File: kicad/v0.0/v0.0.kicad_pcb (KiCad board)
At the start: 2 copper layers, 62 parts, among them J1 USB_B_Micro, J2 9V_IN, J3 LED, J4 MOTOR, J5 LED, J6 MOTOR, Q1 IRF520, Q2 IRF520, SW1 SW_Push, SW2 SW_Push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

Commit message: forgot to save | ready to design PCB
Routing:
- net /3V3: track 34.5 -> 0.00 mm
- net (no net): track 0.00 -> 0.55 mm

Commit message: ab to start pcb design
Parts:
- moved TP5 43.3 mm to (115.0, 88.0)
- moved TP10 42.8 mm to (115.0, 93.0)
- moved TP6 37.5 mm to (119.5, 93.2)
- moved TP9 37.1 mm to (119.5, 97.9)
- moved TP3 37.1 mm to (115.0, 97.8)
- moved TP4 36.9 mm to (119.7, 88.2)
- moved J3 36.2 mm to (204.0, 96.7)
- moved TP7 35.4 mm to (127.9, 88.2)
- moved TP12 33.3 mm to (123.7, 88.0)
- moved U3 32.7 mm to (235.7, 82.5)
- moved TP1 30.6 mm to (123.7, 93.0)
- moved TP2 30.1 mm to (123.7, 98.0)
- moved TP11 28.8 mm to (128.0, 93.1)
- moved TP8 27.5 mm to (128.0, 98.0)
- moved C4 25.1 mm to (275.0, 87.5)
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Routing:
- net +9V: track 56.2 -> 5.74 mm
- net Net-(D5-Pad1): track 35.1 -> 5.32 mm
- net +5V: track 12.9 -> 3.95 mm

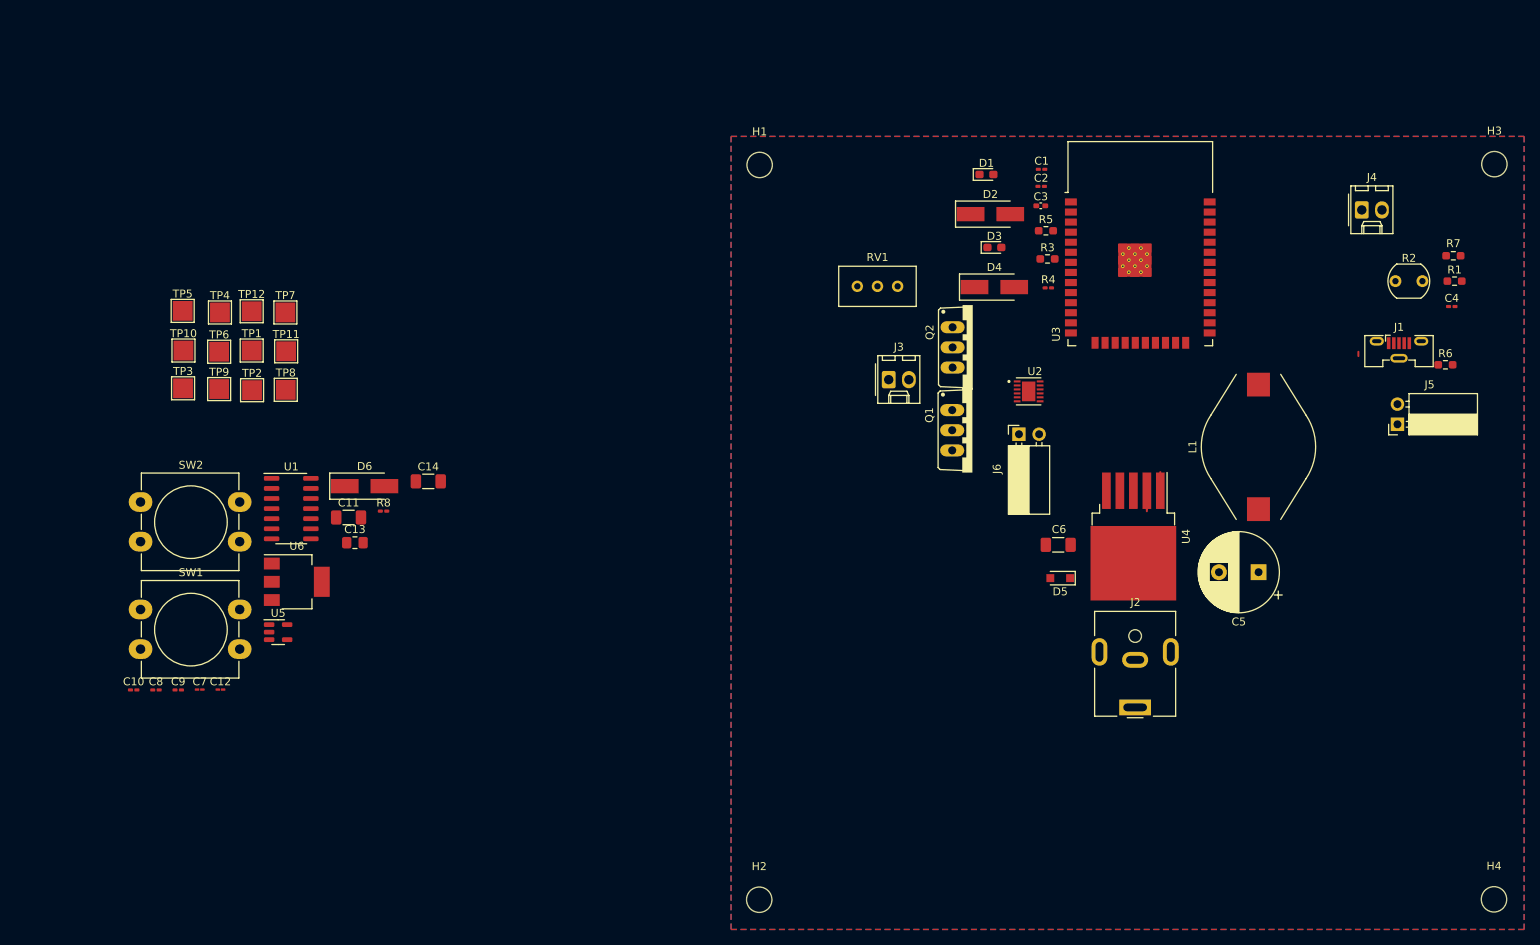
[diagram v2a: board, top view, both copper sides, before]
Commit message: pcb is laid out, time to route
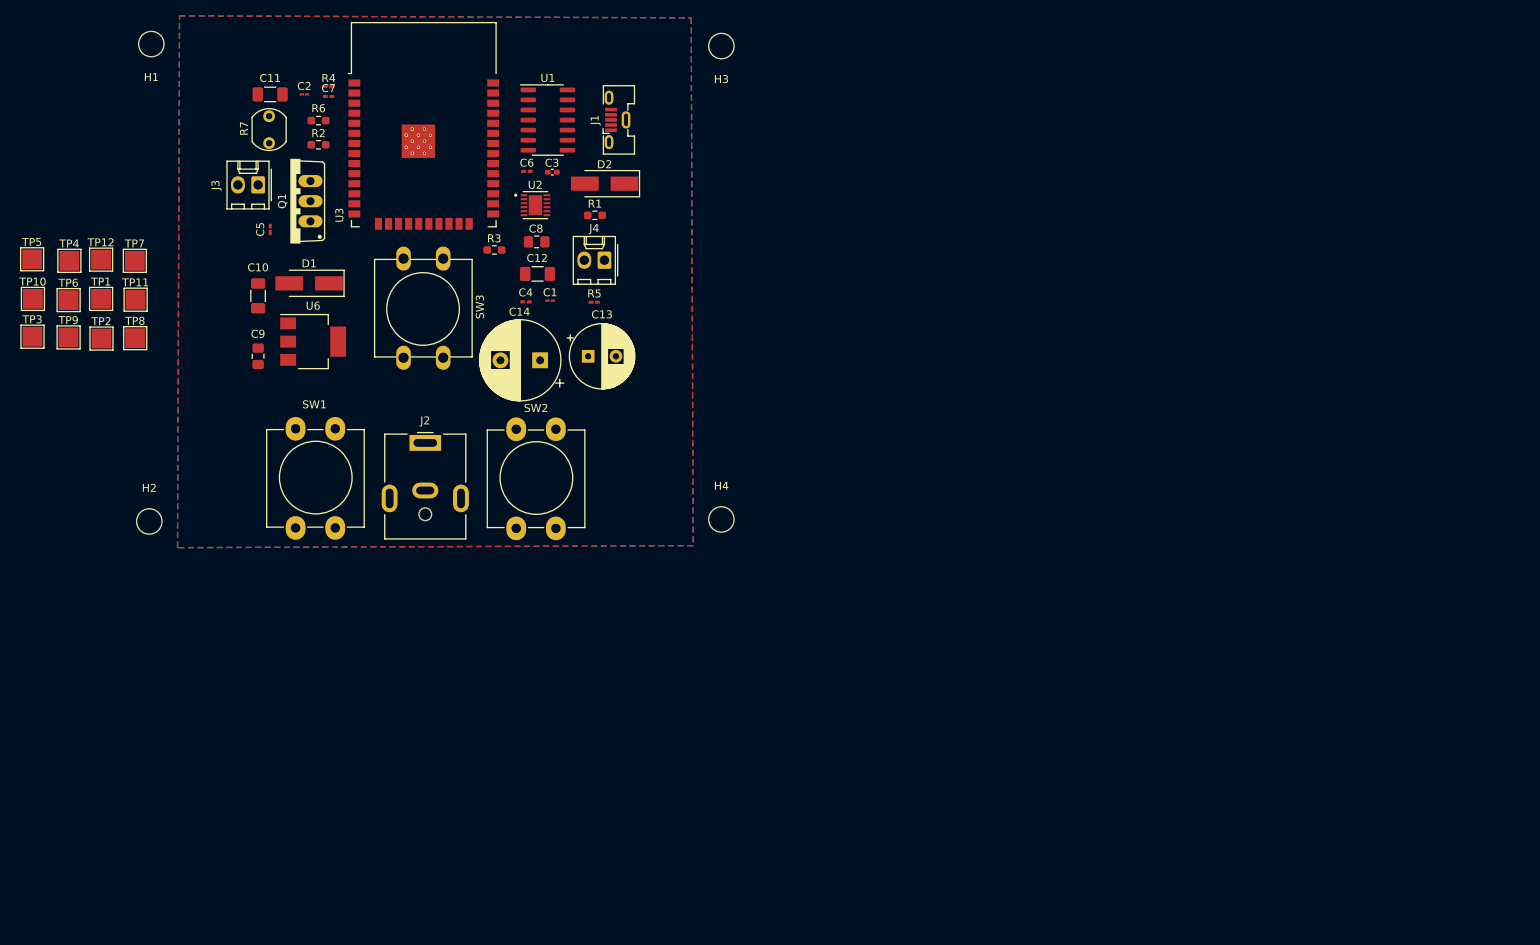
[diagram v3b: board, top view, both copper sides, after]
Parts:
- removed D3: LED, LED_SMD:LED_0603_1608Metric_Pad1.05x0.95mm_HandSolder
- removed D4, D6: D, Diode_SMD:D_SMA_Handsoldering
- removed D5: D_Schottky, Diode_SMD:D_SOD-323_HandSoldering
- removed J5: LED, Connector_PinSocket_2.54mm:PinSocket_1x02_P2.54mm_Horizontal
- removed J6: MOTOR, Connector_PinSocket_2.54mm:PinSocket_1x02_P2.54mm_Horizontal
- removed L1: 68u, Inductor_SMD:L_Bourns_SDR1806
- removed Q2: IRF520, IRF520:TO220BV
- removed R8: 10k, Resistor_SMD:R_0201_0603Metric_Pad0.64x0.40mm_HandSolder
- removed RV1: 100k, Potentiometer_THT:Potentiometer_Bourns_3296W_Vertical
- removed U4: LM2596S-5, Package_TO_SOT_SMD:TO-263-5_TabPin3
- removed U5: AP2112K-3.3, Package_TO_SOT_SMD:SOT-23-5
- added SW3: OPEN/CLOSE, Button_Switch_THT:SW_PUSH-12mm, F.Cu at (147.8, 81.4)
- C1, C2: value 1u -> .1u; footprint Capacitor_SMD:C_0201_0603Metric_Pad0.64x0.40mm_HandSolder -> Capacitor_SMD:C_01005_0402Metric_Pad0.57x0.30mm_HandSolder
- C10: value 1u -> 22u; footprint Capacitor_SMD:C_0201_0603Metric_Pad0.64x0.40mm_HandSolder -> Capacitor_SMD:C_1206_3216Metric_Pad1.33x1.80mm_HandSolder
- C12: value .1u -> 22u; footprint Capacitor_SMD:C_01005_0402Metric_Pad0.57x0.30mm_HandSolder -> Capacitor_SMD:C_1206_3216Metric_Pad1.33x1.80mm_HandSolder
- C13: value 10u -> 220u; footprint Capacitor_SMD:C_0805_2012Metric_Pad1.18x1.45mm_HandSolder -> Capacitor_THT:CP_Radial_D8.0mm_P3.50mm
- C14: value 22u -> 470u; footprint Capacitor_SMD:C_1206_3216Metric_Pad1.33x1.80mm_HandSolder -> Capacitor_THT:CP_Radial_D10.0mm_P5.00mm
- C5: value 470u -> 1u; footprint Capacitor_THT:CP_Radial_D10.0mm_P5.00mm -> Capacitor_SMD:C_0201_0603Metric_Pad0.64x0.40mm_HandSolder
- C6: value 220u -> 1u; footprint Capacitor_SMD:C_1206_3216Metric_Pad1.33x1.80mm_HandSolder -> Capacitor_SMD:C_0201_0603Metric_Pad0.64x0.40mm_HandSolder
- C7: value .1u -> 1u; footprint Capacitor_SMD:C_01005_0402Metric_Pad0.57x0.30mm_HandSolder -> Capacitor_SMD:C_0201_0603Metric_Pad0.64x0.40mm_HandSolder
- C8, C9: value 1u -> 10u; footprint Capacitor_SMD:C_0201_0603Metric_Pad0.64x0.40mm_HandSolder -> Capacitor_SMD:C_0805_2012Metric_Pad1.18x1.45mm_HandSolder
- D1: value LED -> D; footprint LED_SMD:LED_0603_1608Metric_Pad1.05x0.95mm_HandSolder -> Diode_SMD:D_SMA_Handsoldering
- R1: value 20k -> 1k
- R2: value R_Photo -> 1k; footprint OptoDevice:R_LDR_5.1x4.3mm_P3.4mm_Vertical -> Resistor_SMD:R_0603_1608Metric_Pad0.98x0.95mm_HandSolder
- R5: value 1k -> 10k; footprint Resistor_SMD:R_0603_1608Metric_Pad0.98x0.95mm_HandSolder -> Resistor_SMD:R_0201_0603Metric_Pad0.64x0.40mm_HandSolder
- R6: value 1k -> 20k
- R7: value 1k -> R_Photo; footprint Resistor_SMD:R_0603_1608Metric_Pad0.98x0.95mm_HandSolder -> OptoDevice:R_LDR_5.1x4.3mm_P3.4mm_Vertical
- SW1: value SW_Push -> RST
- SW2: value SW_Push -> FLASH
- moved R7 150.4 mm to (125.8, 63.5), turned to -90 degrees
- moved R6 145.4 mm to (132.1, 64.0)
- moved R2 136.9 mm to (132.1, 67.1)
- moved C5 131.9 mm to (126.0, 77.7), turned to -90 degrees
- moved C4 116.7 mm to (158.2, 86.9), turned to 180 degrees
- moved R1 108.7 mm to (166.9, 76.0)
- moved H4 108.6 mm to (182.9, 114.3)
- moved J1 102.7 mm to (169.8, 63.9), turned to 90 degrees
- moved H3 98.6 mm to (182.9, 54.6), turned to 180 degrees
- moved J4 95.7 mm to (168.1, 81.6), turned to 180 degrees
- moved J2 95.5 mm to (145.5, 104.6), turned to 0 degrees
- moved R4 94.2 mm to (133.3, 59.7)
- moved C2 93.6 mm to (130.3, 60.7), turned to 180 degrees
- moved U3 91.6 mm to (145.3, 67.5)
- moved Q1 90.7 mm to (128.5, 74.2), turned to 90 degrees
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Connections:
- net /flash renamed Net-(SW2-Pad1)
- C1 pad 1: Net-(C1-Pad1) -> +9V
- C10 pad 1: Net-(C10-Pad1) -> Net-(D1-Pad2)
- C12 pad 1: +3V3 -> +9V
- C14 pad 1: Net-(C14-Pad1) -> +9V
- C2 pad 1: +9V -> +3V3
- C5 pad 1: GND -> +9V
- C5 pad 2: +9V -> GND
- C6 pad 1: +5V -> Net-(C6-Pad1)
- C8 pad 1: Net-(C7-Pad1) -> +9V
- C9 pad 1: +5V -> +9V
- D1 pad 1: GND -> +3V3
- J1 pad 1: Net-(C1-Pad1) -> Net-(C6-Pad1)
- R1 pad 1: Net-(R1-Pad1) -> /SNS
- R2 pad 1: +3V3 -> Net-(R6-Pad1)
- R2 pad 2: Net-(R1-Pad1) -> /V_PHOTO
- R3 pad 1: /SNS -> GND
- R3 pad 2: GND -> Net-(SW3-Pad1)
- R4 pad 1: Net-(R4-Pad1) -> +3V3
- R4 pad 2: GND -> Net-(C7-Pad1)
- R5 pad 2: Net-(D1-Pad2) -> GND
- R6 pad 2: Net-(D3-Pad2) -> GND
- R7 pad 1: Net-(R1-Pad1) -> +3V3
- R7 pad 2: /V_PHOTO -> Net-(R6-Pad1)
- U1 pad 1: Net-(C1-Pad1) -> Net-(C6-Pad1)
- U1 pad 2: Net-(R6-Pad1) -> unconnected-(U1-Pad2)
- U1 pad 3: Net-(R5-Pad1) -> unconnected-(U1-Pad3)
- U2 pad 8: Net-(R4-Pad1) -> Net-(R5-Pad1)
- U3 pad 27: /open/close button (input) -> Net-(SW3-Pad1)
- U3 pad 28: /led (output) -> /LED
- U3 pad 30: /FWD -> /REV
- U3 pad 31: /REV -> /FWD
- U6 pad 2: Net-(C14-Pad1) -> Net-(D1-Pad2)
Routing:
- net +9V: track 5.74 -> 0.00 mm
- net Net-(D5-Pad1): track 5.32 -> 0.00 mm
- net +5V: track 3.95 -> 0.00 mm
- net Net-(SW3-Pad1): track 0.00 -> 1.11 mm
- net +3V3: track 0.00 -> 0.89 mm
- net (no net): track 0.55 -> 0.00 mm

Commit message: minor tweaks, im a lil bit of a control freak so i keep messing wit it
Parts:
- moved R2 0.76 mm to (132.1, 67.8)
- moved C7 0.60 mm to (133.3, 61.6)
- moved R6 0.51 mm to (132.1, 64.5)
- moved R4 0.25 mm to (133.3, 59.4)
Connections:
- R3 pad 2: Net-(SW3-Pad1) -> Net-(R3-Pad2)
- SW3 pad 1: Net-(SW3-Pad1) -> GND
- U3 pad 27: Net-(SW3-Pad1) -> Net-(R3-Pad2)
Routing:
- net Net-(SW3-Pad1): track 1.11 -> 0.00 mm
- net GND: track 0.00 -> 1.11 mm
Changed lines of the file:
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@@
   (net 63 "unconnected-(U3-Pad36)")
   (net 64 "unconnected-(U3-Pad37)")
-  (net 65 "Net-(SW3-Pad1)")
-  (net 66 "Net-(SW2-Pad1)")
-  (net 67 "Net-(R6-Pad1)")
-  (net 68 "Net-(R5-Pad1)")
-  (net 69 "unconnected-(U1-Pad2)")
-  (net 70 "unconnected-(U1-Pad3)")
+  (net 65 "Net-(SW2-Pad1)")
+  (net 66 "Net-(R6-Pad1)")
+  (net 67 "Net-(R5-Pad1)")
+  (net 68 "unconnected-(U1-Pad2)")
+  (net 69 "unconnected-(U1-Pad3)")
+  (net 70 "Net-(R3-Pad2)")
   (footprint "Capacitor_SMD:C_0201_0603Metric_Pad0.64x0.40mm_HandSolder" (layer "F.Cu")
     (at 125.984 77.724 -90)
@@
     (fp_line (start 12.25 -3.5) (end 12.25 8.5) (layer "F.Fab") (width 0.1))
     (pad "1" thru_hole oval (at 12.5 0 270) (size 3.048 1.85) (drill 1.3) (layers *.Cu *.Mask)
-      (net 65 "Net-(SW3-Pad1)") (pinfunction "1") (pintype "passive"))
+      (net 2 "GND") (pinfunction "1") (pintype "passive"))
     (pad "1" thru_hole oval (at 0 0 270) (size 3.048 1.85) (drill 1.3) (layers *.Cu *.Mask)
-      (net 65 "Net-(SW3-Pad1)") (pinfunction "1") (pintype "passive"))
+      (net 2 "GND") (pinfunction "1") (pintype "passive"))
     (pad "2" thru_hole oval (at 0 5 270) (size 3.048 1.85) (drill 1.3) (layers *.Cu *.Mask)
       (net 9 "+3V3") (pinfunction "2") (pintype "passive"))
@@
   )
   (footprint "Resistor_SMD:R_0603_1608Metric_Pad0.98x0.95mm_HandSolder" (layer "F.Cu")
-    (at 132.08 64.008)
+    (at 132.08 64.516)
     (descr "Resistor SMD 0603 (1608 Metric), square (rectangular) end terminal, IPC_7351 nominal with elongated pad for handsoldering. (Body size source: IPC-SM-782 page 72, https://www.pcb-3d.com/wordpress/wp-content/uploads/ipc-sm-782a_amendment_1_and_2.pdf), generated with kicad-footprint-generator")
     (tags "resistor handsolder")
@@
     (fp_line (start -0.8 0.4125) (end -0.8 -0.4125) (layer "F.Fab") (width 0.1))
     (pad "1" smd roundrect (at -0.9125 0) (size 0.975 0.95) (layers "F.Cu" "F.Paste" "F.Mask") (roundrect_rratio 0.25)
-      (net 67 "Net-(R6-Pad1)") (pintype "passive"))
+      (net 66 "Net-(R6-Pad1)") (pintype "passive"))
     (pad "2" smd roundrect (at 0.9125 0) (size 0.975 0.95) (layers "F.Cu" "F.Paste" "F.Mask") (roundrect_rratio 0.25)
       (net 2 "GND") (pintype "passive"))
@@
       (net 59 "Net-(C6-Pad1)") (pinfunction "VDD") (pintype "power_in"))
     (pad "2" smd roundrect (at -2.475 -2.54) (size 1.95 0.6) (layers "F.Cu" "F.Paste" "F.Mask") (roundrect_rratio 0.25)
-      (net 69 "unconnected-(U1-Pad2)") (pinfunction "GP0") (pintype "bidirectional"))
+      (net 68 "unconnected-(U1-Pad2)") (pinfunction "GP0") (pintype "bidirectional"))
     (pad "3" smd roundrect (at -2.475 -1.27) (size 1.95 0.6) (layers "F.Cu" "F.Paste" "F.Mask") (roundrect_rratio 0.25)
-      (net 70 "unconnected-(U1-Pad3)") (pinfunction "GP1") (pintype "bidirectional"))
+      (net 69 "unconnected-(U1-Pad3)") (pinfunction "GP1") (pintype "bidirectional"))
     (pad "4" smd roundrect (at -2.475 0) (size 1.95 0.6) (layers "F.Cu" "F.Paste" "F.Mask") (roundrect_rratio 0.25)
       (net 31 "unconnected-(U1-Pad4)") (pinfunction "~{RST}") (pintype "input"))
@@
     (fp_line (start 0.25 -3.5) (end 0.25 8.5) (layer "F.Fab") (width 0.1))
     (pad "1" thru_hole oval (at 12.5 0 90) (size 3 2.5) (drill 1.2) (layers *.Cu *.Mask)
-      (net 66 "Net-(SW2-Pad1)") (pinfunction "1") (pintype "passive"))
+      (net 65 "Net-(SW2-Pad1)") (pinfunction "1") (pintype "passive"))
     (pad "1" thru_hole oval (at 0 0 90) (size 3 2.5) (drill 1.2) (layers *.Cu *.Mask)
-      (net 66 "Net-(SW2-Pad1)") (pinfunction "1") (pintype "passive"))
+      (net 65 "Net-(SW2-Pad1)") (pinfunction "1") (pintype "passive"))
     (pad "2" thru_hole oval (at 12.5 5 90) (size 3 2.5) (drill 1.2) (layers *.Cu *.Mask)
       (net 2 "GND") (pinfunction "2") (pintype "passive"))
@@
       (net 2 "GND") (pintype "passive"))
     (pad "2" smd roundrect (at 0.9125 0 180) (size 0.975 0.95) (layers "F.Cu" "F.Paste" "F.Mask") (roundrect_rratio 0.25)
-      (net 65 "Net-(SW3-Pad1)") (pintype "passive"))
+      (net 70 "Net-(R3-Pad2)") (pintype "passive"))
     (model "${KICAD6_3DMODEL_DIR}/Resistor_SMD.3dshapes/R_0603_1608Metric.wrl"
       (offset (xyz 0 0 0))
@@
   )
   (footprint "Capacitor_SMD:C_0201_0603Metric_Pad0.64x0.40mm_HandSolder" (layer "F.Cu")
-    (at 133.35 60.96 180)
+    (at 133.35 61.564 180)
     (descr "Capacitor SMD 0201 (0603 Metric), square (rectangular) end terminal, IPC_7351 nominal with elongated pad for handsoldering. (Body size source: https://www.vishay.com/docs/20052/crcw0201e3.pdf), generated with kicad-footprint-generator")
     (tags "capacitor handsolder")
@@
     (pad "" smd roundrect (at 0.4325 0) (size 0.458 0.36) (layers "F.Paste") (roundrect_rratio 0.25))
     (pad "1" smd roundrect (at -0.4075 0) (size 0.635 0.4) (layers "F.Cu" "F.Mask") (roundrect_rratio 0.25)
-      (net 68 "Net-(R5-Pad1)") (pintype "passive"))
+      (net 67 "Net-(R5-Pad1)") (pintype "passive"))
     (pad "2" smd roundrect (at 0.4075 0) (size 0.635 0.4) (layers "F.Cu" "F.Mask") (roundrect_rratio 0.25)
       (net 2 "GND") (pintype "passive"))
@@
   )
   (footprint "Resistor_SMD:R_0603_1608Metric_Pad0.98x0.95mm_HandSolder" (layer "F.Cu")
-    (at 132.08 67.056)
+    (at 132.08 67.818)
     (descr "Resistor SMD 0603 (1608 Metric), square (rectangular) end terminal, IPC_7351 nominal with elongated pad for handsoldering. (Body size source: IPC-SM-782 page 72, https://www.pcb-3d.com/wordpress/wp-content/uploads/ipc-sm-782a_amendment_1_and_2.pdf), generated with kicad-footprint-generator")
     (tags "resistor handsolder")
@@
     (fp_line (start 0.8 -0.4125) (end 0.8 0.4125) (layer "F.Fab") (width 0.1))
     (pad "1" smd roundrect (at -0.9125 0) (size 0.975 0.95) (layers "F.Cu" "F.Paste" "F.Mask") (roundrect_rratio 0.25)
-      (net 67 "Net-(R6-Pad1)") (pintype "passive"))
+      (net 66 "Net-(R6-Pad1)") (pintype "passive"))
     (pad "2" smd roundrect (at 0.9125 0) (size 0.975 0.95) (layers "F.Cu" "F.Paste" "F.Mask") (roundrect_rratio 0.25)
       (net 7 "/V_PHOTO") (pintype "passive"))
@@
       (net 57 "unconnected-(U3-Pad24)") (pinfunction "IO2") (pintype "bidirectional"))
     (pad "25" smd rect (at 8.75 8.26) (size 1.5 0.9) (layers "F.Cu" "F.Paste" "F.Mask")
-      (net 66 "Net-(SW2-Pad1)") (pinfunction "IO0") (pintype "bidirectional"))
+      (net 65 "Net-(SW2-Pad1)") (pinfunction "IO0") (pintype "bidirectional"))
     (pad "26" smd rect (at 8.75 6.99) (size 1.5 0.9) (layers "F.Cu" "F.Paste" "F.Mask")
       (net 58 "unconnected-(U3-Pad26)") (pinfunction "IO4") (pintype "bidirectional"))
     (pad "27" smd rect (at 8.75 5.72) (size 1.5 0.9) (layers "F.Cu" "F.Paste" "F.Mask")
-      (net 65 "Net-(SW3-Pad1)") (pinfunction "IO16") (pintype "bidirectional"))
+      (net 70 "Net-(R3-Pad2)") (pinfunction "IO16") (pintype "bidirectional"))
     (pad "28" smd rect (at 8.75 4.45) (size 1.5 0.9) (layers "F.Cu" "F.Paste" "F.Mask")
       (net 17 "/LED") (pinfunction "IO17") (pintype "bidirectional"))
@@
   )
   (footprint "Resistor_SMD:R_0201_0603Metric_Pad0.64x0.40mm_HandSolder" (layer "F.Cu")
-    (at 133.35 59.69)
+    (at 133.35 59.436)
     (descr "Resistor SMD 0201 (0603 Metric), square (rectangular) end terminal, IPC_7351 nominal with elongated pad for handsoldering. (Body size source: https://www.vishay.com/docs/20052/crcw0201e3.pdf), generated with kicad-footprint-generator")
     (tags "resistor handsolder")
@@
       (net 38 "unconnected-(U2-Pad7)") (pinfunction "~{FAULT}") (pintype "output"))
     (pad "8" smd roundrect locked (at 1.445 0.75) (size 0.84 0.27) (layers "F.Cu" "F.Paste" "F.Mask") (roundrect_rratio 0.03)
-      (net 68 "Net-(R5-Pad1)") (pinfunction "~{EN}") (pintype "input"))
+      (net 67 "Net-(R5-Pad1)") (pinfunction "~{EN}") (pintype "input"))
     (pad "9" smd roundrect locked (at 1.445 0.25) (size 0.84 0.27) (layers "F.Cu" "F.Paste" "F.Mask") (roundrect_rratio 0.03)
       (net 2 "GND") (pinfunction "GND") (pintype "power_in"))
@@
       (net 9 "+3V3") (pintype "passive"))
     (pad "2" thru_hole circle (at 3.4 0 270) (size 1.5 1.5) (drill 0.8) (layers *.Cu *.Mask)
-      (net 67 "Net-(R6-Pad1)") (pintype "passive"))
+      (net 66 "Net-(R6-Pad1)") (pintype "passive"))
     (model "${KICAD6_3DMODEL_DIR}/OptoDevice.3dshapes/R_LDR_5.1x4.3mm_P3.4mm_Vertical.wrl"
       (offset (xyz 0 0 0))
@@
     (style (thickness 0.2) (arrow_length 1.27) (text_position_mode 0) (extension_height 0.58642) (extension_offset 0.5) keep_text_aligned)
   )
+  (segment (start 147.8 80.3) (end 147.8 81.41) (width 0.25) (layer "F.Cu") (net 2))
   (segment (start 136.2475 62.1575) (end 136.6 61.805) (width 0.25) (layer "F.Cu") (net 8))
   (segment (start 142.8 81.64) (end 142.8 80.75) (width 0.25) (layer "F.Cu") (net 9))
-  (segment (start 147.8 80.3) (end 147.8 81.41) (width 0.25) (layer "F.Cu") (net 65))
   (zone (net 2) (net_name "GND") (layers F&B.Cu) (hatch edge 0.508)
     (connect_pads (clearance 0.508))
     (min_thickness 0.254) (filled_areas_thickness no)
-    (fill (thermal_gap 0.508) (thermal_bridge_width 0.508))
+    (fill yes (thermal_gap 0.508) (thermal_bridge_width 0.508))
     (polygon
       (pts

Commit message: pcb v1
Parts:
- moved R6 0.11 mm to (132.0, 64.6)
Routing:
- net GND: track 1.11 -> 265.4 mm, vias 0 -> 4
- net +9V: track 0.00 -> 179.3 mm, vias 0 -> 6
- net +3V3: track 0.89 -> 133.9 mm, vias 0 -> 3
- net Net-(C7-Pad1): track 0.50 -> 62.9 mm, vias 0 -> 2
- net Net-(SW2-Pad1): track 0.00 -> 42.3 mm, vias 0 -> 2
- net /LED: track 0.00 -> 28.3 mm, vias 0 -> 2
- net /SNS: track 0.00 -> 27.6 mm, vias 0 -> 2
- net Net-(C6-Pad1): track 0.00 -> 21.5 mm
- net Net-(J4-Pad1): track 0.00 -> 19.1 mm, vias 0 -> 1
- net /REV: track 0.00 -> 17.6 mm, vias 0 -> 2
- net Net-(D1-Pad2): track 0.00 -> 17.4 mm, vias 0 -> 2
- net Net-(R5-Pad1): track 0.00 -> 14.3 mm
- net Net-(C3-Pad1): track 0.00 -> 13.3 mm
- net /FWD: track 0.00 -> 12.9 mm, vias 0 -> 2
- net Net-(J4-Pad2): track 0.00 -> 10.4 mm
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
